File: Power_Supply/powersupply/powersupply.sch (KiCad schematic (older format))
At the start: 68 parts, among them J1 Conn_01x03, J2 USB_B_Micro, J3 1x2, Q1 Q_PMOS_GDS, SW1 KMR2, U1 AZ1117E-3.3, U10 INA199, U2 ATSAMD10D13A-SS, U3 B0505S-2WR2, U4 TFT_OLED, U5 joystick-K1-1506DN-01, U6 MC33063AP1, U7 LM358P, U8 1x2

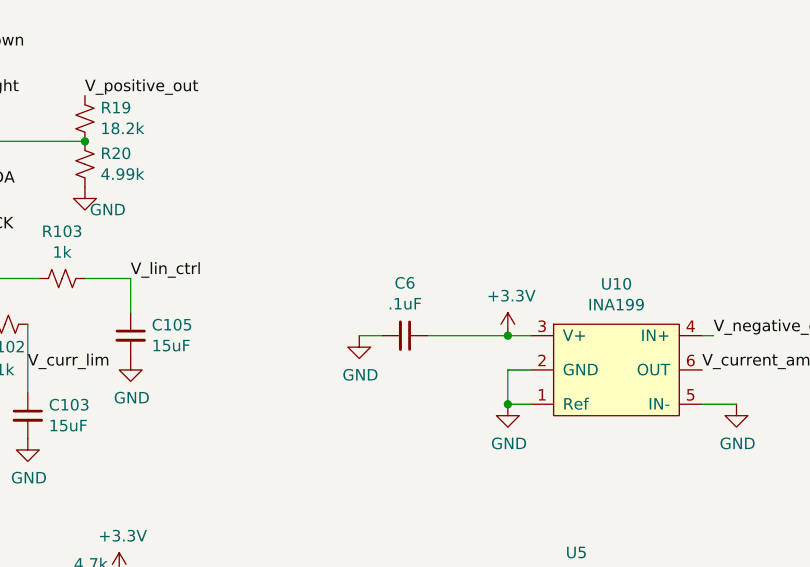
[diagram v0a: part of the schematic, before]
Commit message: new layout for power supply
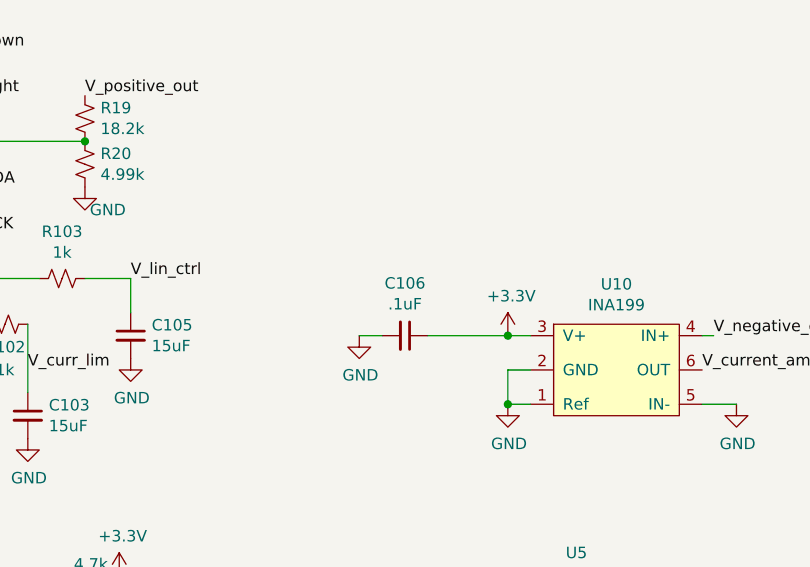
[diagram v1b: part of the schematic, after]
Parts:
- C106: renamed from C6; footprint Capacitor_THT:C_Rect_L4.0mm_W2.5mm_P2.50mm -> Capacitor_SMD:C_0805_2012Metric
- D4: footprint LED_THT:LED_D3.0mm_Horizontal_O1.27mm_Z6.0mm -> LED_THT:LED_D3.0mm
- U7: footprint powersupply:LM358P -> Package_DIP:DIP-8_W7.62mm
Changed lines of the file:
@@
 F 0 "U7" H 8375 3265 50  0000 C CNN
 F 1 "LM358P" H 8375 3174 50  0000 C CNN
-F 2 "powersupply:LM358P" H 8400 3150 50  0001 C CNN
+F 2 "Package_DIP:DIP-8_W7.62mm" H 8400 3150 50  0001 C CNN
 F 3 "" H 8400 3150 50  0001 C CNN
 	1    8400 3150
@@
 F 0 "D4" V 3389 1082 50  0000 R CNN
 F 1 "C503B 2.1V" V 3298 1082 50  0000 R CNN
-F 2 "LED_THT:LED_D3.0mm_Horizontal_O1.27mm_Z6.0mm" H 3350 1200 50  0001 C CNN
+F 2 "LED_THT:LED_D3.0mm" H 3350 1200 50  0001 C CNN
 F 3 "~" H 3350 1200 50  0001 C CNN
 	1    3350 1200
@@
 Connection ~ 4700 6150
 $Comp
-L Device:C_Small C6
+L Device:C_Small C106
 U 1 1 5D675D51
 P 4250 5850
-F 0 "C6" V 4021 5850 50  0000 C CNN
+F 0 "C106" V 4021 5850 50  0000 C CNN
 F 1 ".1uF" V 4112 5850 50  0000 C CNN
-F 2 "Capacitor_THT:C_Rect_L4.0mm_W2.5mm_P2.50mm" H 4250 5850 50  0001 C CNN
+F 2 "Capacitor_SMD:C_0805_2012Metric" H 4250 5850 50  0001 C CNN
 F 3 "~" H 4250 5850 50  0001 C CNN
 	1    4250 5850

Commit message: big CHANGES
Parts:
- R1: footprint Resistor_THT:R_Axial_DIN0207_L6.3mm_D2.5mm_P10.16mm_Horizontal -> Resistor_SMD:R_0805_2012Metric
- R18: footprint Resistor_SMD:R_0805_2012Metric -> Resistor_THT:R_Axial_DIN0207_L6.3mm_D2.5mm_P10.16mm_Horizontal
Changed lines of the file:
@@
 F 0 "R1" V 2450 1200 50  0000 C CNN
 F 1 "150" V 2536 1200 50  0000 C CNN
-F 2 "Resistor_THT:R_Axial_DIN0207_L6.3mm_D2.5mm_P10.16mm_Horizontal" H 2650 1200 50  0001 C CNN
+F 2 "Resistor_SMD:R_0805_2012Metric" H 2650 1200 50  0001 C CNN
 F 3 "~" H 2650 1200 50  0001 C CNN
 	1    2650 1200
@@
 F 0 "R18" H 3418 946 50  0000 L CNN
 F 1 "300" H 3418 855 50  0000 L CNN
-F 2 "Resistor_SMD:R_0805_2012Metric" H 3350 900 50  0001 C CNN
+F 2 "Resistor_THT:R_Axial_DIN0207_L6.3mm_D2.5mm_P10.16mm_Horizontal" H 3350 900 50  0001 C CNN
 F 3 "~" H 3350 900 50  0001 C CNN
 	1    3350 900

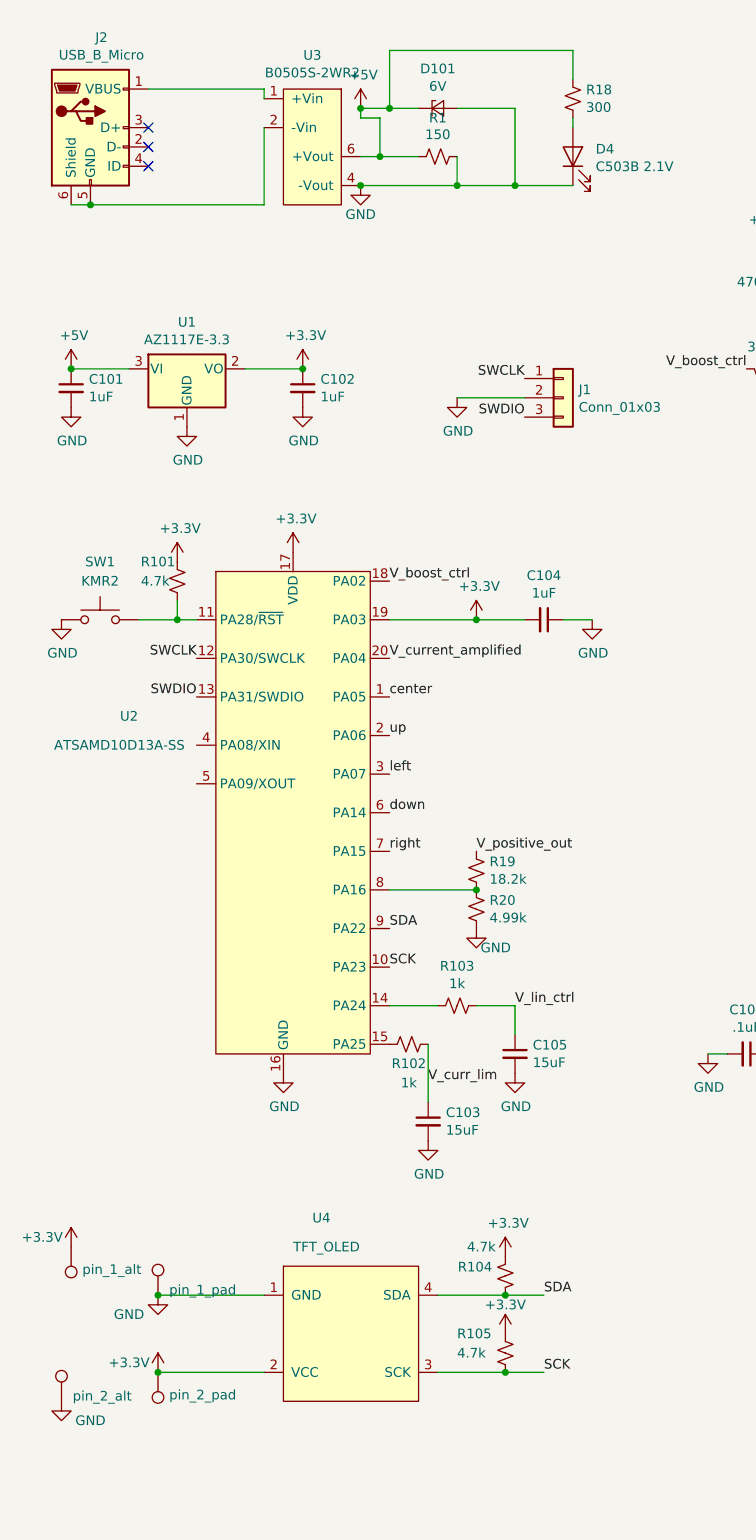
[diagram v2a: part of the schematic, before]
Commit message: new layout with SMD components
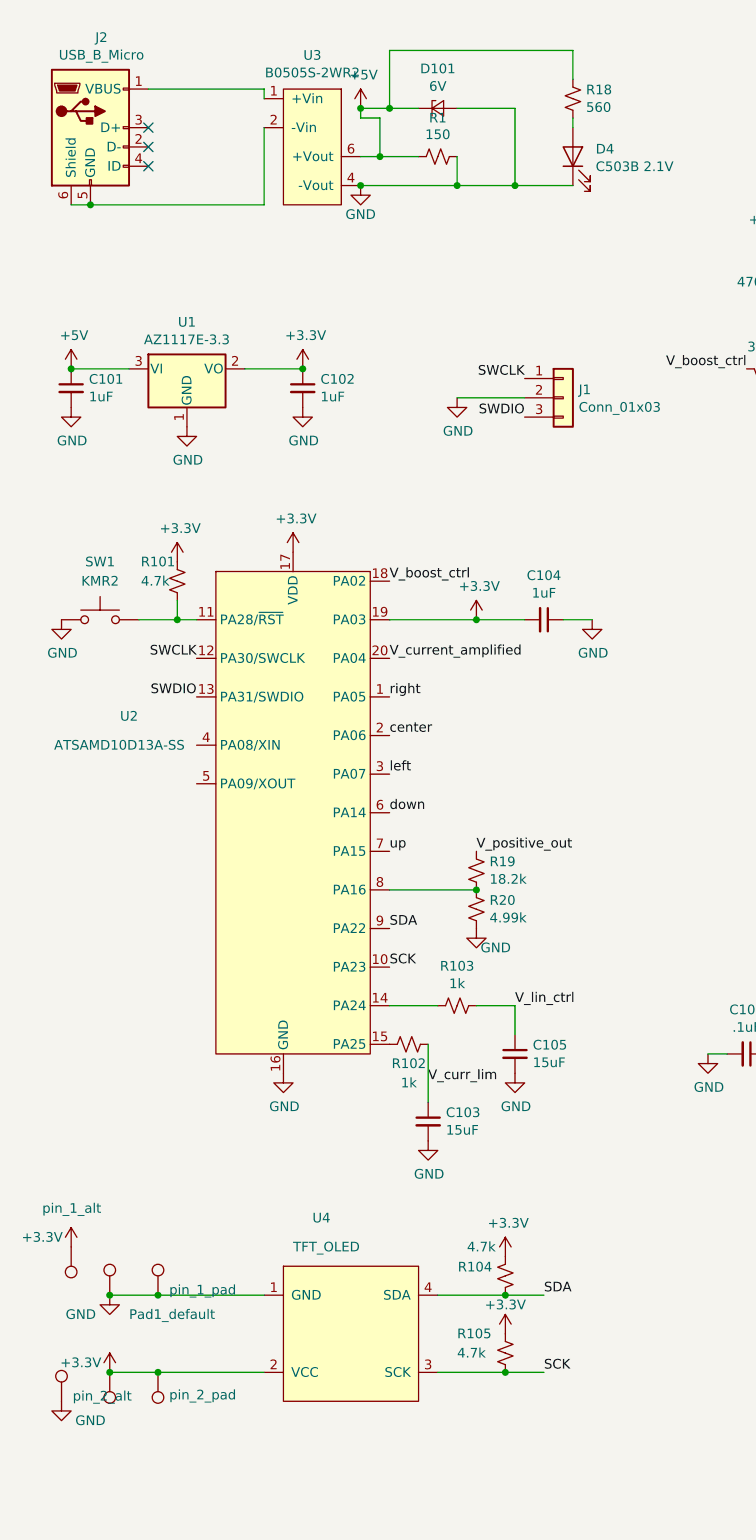
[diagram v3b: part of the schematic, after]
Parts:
- added TP12: Pad1_default, powersupply:pads, symbol Connector:TestPoint
- added TP13: TestPoint, powersupply:pads, symbol Connector:TestPoint
- R18: value 300 -> 560
- TP1, TP2, TP3, TP4, TP5, TP6, TP7: footprint Connector_PinSocket_2.54mm:PinSocket_1x01_P2.54mm_Vertical -> Connector_PinHeader_1.00mm:PinHeader_1x01_P1.00mm_Vertical
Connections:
- net +3V3: now also TP13.1
- net GND: now also TP12.1
- net center: now also U2.2 (PA06); no longer U2.1 (PA05)
- net right: now also U2.1 (PA05); no longer U2.7 (PA15)
- net up: now also U2.7 (PA15); no longer U2.2 (PA06)
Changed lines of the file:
@@
 $EndComp
 Text Label 2400 4200 0    50   ~ 0
-up
+center
 Text Label 2400 4400 0    50   ~ 0
 left
@@
 down
 Text Label 2400 4000 0    50   ~ 0
-center
+right
 Text Label 4550 7100 2    50   ~ 0
 up
@@
 Connection ~ 3000 7500
 Text Label 2400 4800 0    50   ~ 0
-right
+up
 Wire Wire Line
 	2750 950  3050 950
@@
 F 0 "TP3" H 9992 826 50  0000 R CNN
 F 1 "+3.3" H 9992 917 50  0000 R CNN
-F 2 "Connector_PinSocket_2.54mm:PinSocket_1x01_P2.54mm_Vertical" H 10250 800 50  0001 C CNN
+F 2 "Connector_PinHeader_1.00mm:PinHeader_1x01_P1.00mm_Vertical" H 10250 800 50  0001 C CNN
 F 3 "~" H 10250 800 50  0001 C CNN
 	1    10050 800
@@
 F 0 "TP2" H 10492 826 50  0000 R CNN
 F 1 "+5_isolated" H 10492 917 50  0000 R CNN
-F 2 "Connector_PinSocket_2.54mm:PinSocket_1x01_P2.54mm_Vertical" H 10750 800 50  0001 C CNN
+F 2 "Connector_PinHeader_1.00mm:PinHeader_1x01_P1.00mm_Vertical" H 10750 800 50  0001 C CNN
 F 3 "~" H 10750 800 50  0001 C CNN
 	1    10550 800
@@
 F 0 "TP1" H 10658 1768 50  0000 L CNN
 F 1 "Boost_out" H 10658 1677 50  0000 L CNN
-F 2 "Connector_PinSocket_2.54mm:PinSocket_1x01_P2.54mm_Vertical" H 10800 1650 50  0001 C CNN
+F 2 "Connector_PinHeader_1.00mm:PinHeader_1x01_P1.00mm_Vertical" H 10800 1650 50  0001 C CNN
 F 3 "~" H 10800 1650 50  0001 C CNN
 	1    10600 1650
@@
 F 0 "TP4" H 9608 1518 50  0000 L CNN
 F 1 "Current_limit" H 9608 1427 50  0000 L CNN
-F 2 "Connector_PinSocket_2.54mm:PinSocket_1x01_P2.54mm_Vertical" H 9750 1400 50  0001 C CNN
+F 2 "Connector_PinHeader_1.00mm:PinHeader_1x01_P1.00mm_Vertical" H 9750 1400 50  0001 C CNN
 F 3 "~" H 9750 1400 50  0001 C CNN
 	1    9550 1400
@@
 F 0 "TP5" H 9608 1768 50  0000 L CNN
 F 1 "Voltage_limit" H 9608 1677 50  0000 L CNN
-F 2 "Connector_PinSocket_2.54mm:PinSocket_1x01_P2.54mm_Vertical" H 9750 1650 50  0001 C CNN
+F 2 "Connector_PinHeader_1.00mm:PinHeader_1x01_P1.00mm_Vertical" H 9750 1650 50  0001 C CNN
 F 3 "~" H 9750 1650 50  0001 C CNN
 	1    9550 1650
@@
 F 0 "TP6" H 10658 1518 50  0000 L CNN
 F 1 "Boost_ctrl" H 10658 1427 50  0000 L CNN
-F 2 "Connector_PinSocket_2.54mm:PinSocket_1x01_P2.54mm_Vertical" H 10800 1400 50  0001 C CNN
+F 2 "Connector_PinHeader_1.00mm:PinHeader_1x01_P1.00mm_Vertical" H 10800 1400 50  0001 C CNN
 F 3 "~" H 10800 1400 50  0001 C CNN
 	1    10600 1400
@@
 F 0 "TP7" H 9608 968 50  0000 L CNN
 F 1 "GND" H 9608 877 50  0000 L CNN
-F 2 "Connector_PinSocket_2.54mm:PinSocket_1x01_P2.54mm_Vertical" H 9750 850 50  0001 C CNN
+F 2 "Connector_PinHeader_1.00mm:PinHeader_1x01_P1.00mm_Vertical" H 9750 850 50  0001 C CNN
 F 3 "~" H 9750 850 50  0001 C CNN
 	1    9550 850
@@
 L power:+3.3V #PWR07
 U 1 1 5D56EC9F
-P 1200 7500
-F 0 "#PWR07" H 1200 7350 50  0001 C CNN
-F 1 "+3.3V" H 1050 7550 50  0000 C CNN
-F 2 "" H 1200 7500 50  0001 C CNN
-F 3 "" H 1200 7500 50  0001 C CNN
-	1    1200 7500
+P 950 7500
+F 0 "#PWR07" H 950 7350 50  0001 C CNN
+F 1 "+3.3V" H 800 7550 50  0000 C CNN
+F 2 "" H 950 7500 50  0001 C CNN
+F 3 "" H 950 7500 50  0001 C CNN
+	1    950  7500
 	1    0    0    -1
 $EndComp
@@
 $EndComp
 $Comp
-L power:GND #PWR06
-U 1 1 5D56D783
-P 1200 7100
-F 0 "#PWR06" H 1200 6850 50  0001 C CNN
-F 1 "GND" H 1050 7000 50  0000 C CNN
-F 2 "" H 1200 7100 50  0001 C CNN
-F 3 "" H 1200 7100 50  0001 C CNN
-	1    1200 7100
-	1    0    0    -1
-$EndComp
-$Comp
 L Connector:TestPoint TP11
 U 1 1 5D59533A
@@
 	1    0    0    -1
 $EndComp
-Connection ~ 1200 7500
 $Comp
 L Connector:TestPoint TP10
@@
 	-1   0    0    1
 $EndComp
-Connection ~ 1200 7100
 $Comp
 L Connector:TestPoint TP9
@@
 P 750 6850
 F 0 "TP8" H 692 6876 50  0001 R CNN
-F 1 "pin_1_alt" H 692 6967 50  0000 R CNN
+F 1 "pin_1_alt" H 900 6650 50  0000 R CNN
 F 2 "powersupply:pads" H 950 6850 50  0001 C CNN
 F 3 "~" H 950 6850 50  0001 C CNN
@@
 P 3350 900
 F 0 "R18" H 3418 946 50  0000 L CNN
-F 1 "300" H 3418 855 50  0000 L CNN
+F 1 "560" H 3418 855 50  0000 L CNN
 F 2 "Resistor_THT:R_Axial_DIN0207_L6.3mm_D2.5mm_P10.16mm_Horizontal" H 3350 900 50  0001 C CNN
 F 3 "~" H 3350 900 50  0001 C CNN
@@
 Wire Wire Line
 	10850 4450 10850 4800
+$Comp
+L power:GND #PWR06
+U 1 1 5D56D783
+P 950 7100
+F 0 "#PWR06" H 950 6850 50  0001 C CNN
+F 1 "GND" H 800 7000 50  0000 C CNN
+F 2 "" H 950 7100 50  0001 C CNN
+F 3 "" H 950 7100 50  0001 C CNN
+	1    950  7100
+	1    0    0    -1
+$EndComp
+$Comp
+L Connector:TestPoint TP12
+U 1 1 5D59450B
+P 950 7100
+F 0 "TP12" H 1008 7218 50  0001 L CNN
+F 1 "Pad1_default" H 1050 7000 50  0000 L CNN
+F 2 "powersupply:pads" H 1150 7100 50  0001 C CNN
+F 3 "~" H 1150 7100 50  0001 C CNN
+	1    950  7100
+	1    0    0    -1
+$EndComp
+Wire Wire Line
+	1200 7100 950  7100
+Connection ~ 1200 7100
+Connection ~ 950  7100
+$Comp
+L Connector:TestPoint TP13
+U 1 1 5D5A2114
+P 950 7500
+F 0 "TP13" H 892 7526 50  0001 R CNN
+F 1 "TestPoint" H 892 7617 50  0001 R CNN
+F 2 "powersupply:pads" H 1150 7500 50  0001 C CNN
+F 3 "~" H 1150 7500 50  0001 C CNN
+	1    950  7500
+	-1   0    0    1
+$EndComp
+Wire Wire Line
+	1200 7500 950  7500
+Connection ~ 1200 7500
+Connection ~ 950  7500
 $EndSCHEMATC

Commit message: finished layout
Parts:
- renumbered U8 to J4, U4 to MOD1
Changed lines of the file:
@@
 SDA
 $Comp
-L powersupply:TFT_OLED U4
+L powersupply:TFT_OLED MOD1
 U 1 1 5D37FF21
 P 2050 6700
-F 0 "U4" H 2000 6700 50  0000 L CNN
+F 0 "MOD1" H 2000 6700 50  0000 L CNN
 F 1 "TFT_OLED" H 1900 6550 50  0000 L CNN
 F 2 "powersupply:TFT_OLED_display" H 2050 6700 50  0001 C CNN
@@
 	2750 950  3050 950
 $Comp
-L Connector_Generic:Conn_01x02 U8
+L Connector_Generic:Conn_01x02 J4
 U 1 1 5D4A34EF
 P 10650 4350
-F 0 "U8" H 10600 4000 50  0000 L CNN
+F 0 "J4" H 10600 4000 50  0000 L CNN
 F 1 "1x2" H 10600 4100 50  0000 L CNN
 F 2 "powersupply:Banana Sockets" H 10650 4500 50  0001 C CNN

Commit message: small changes
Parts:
- TP13: value TestPoint -> pin_2_pad_alt
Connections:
- net USB_5V: now reaches J2.1 (VBUS), U3.1 (+Vin)
- net USB_GND: now reaches J2.5 (GND), J2.6 (Shield), U3.2 (-Vin)
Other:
- moved on the sheet: C1, C101, C102, C103, C104, C105, C106, C2, C3, C4, C5, D1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
